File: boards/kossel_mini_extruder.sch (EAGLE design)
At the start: 31 parts

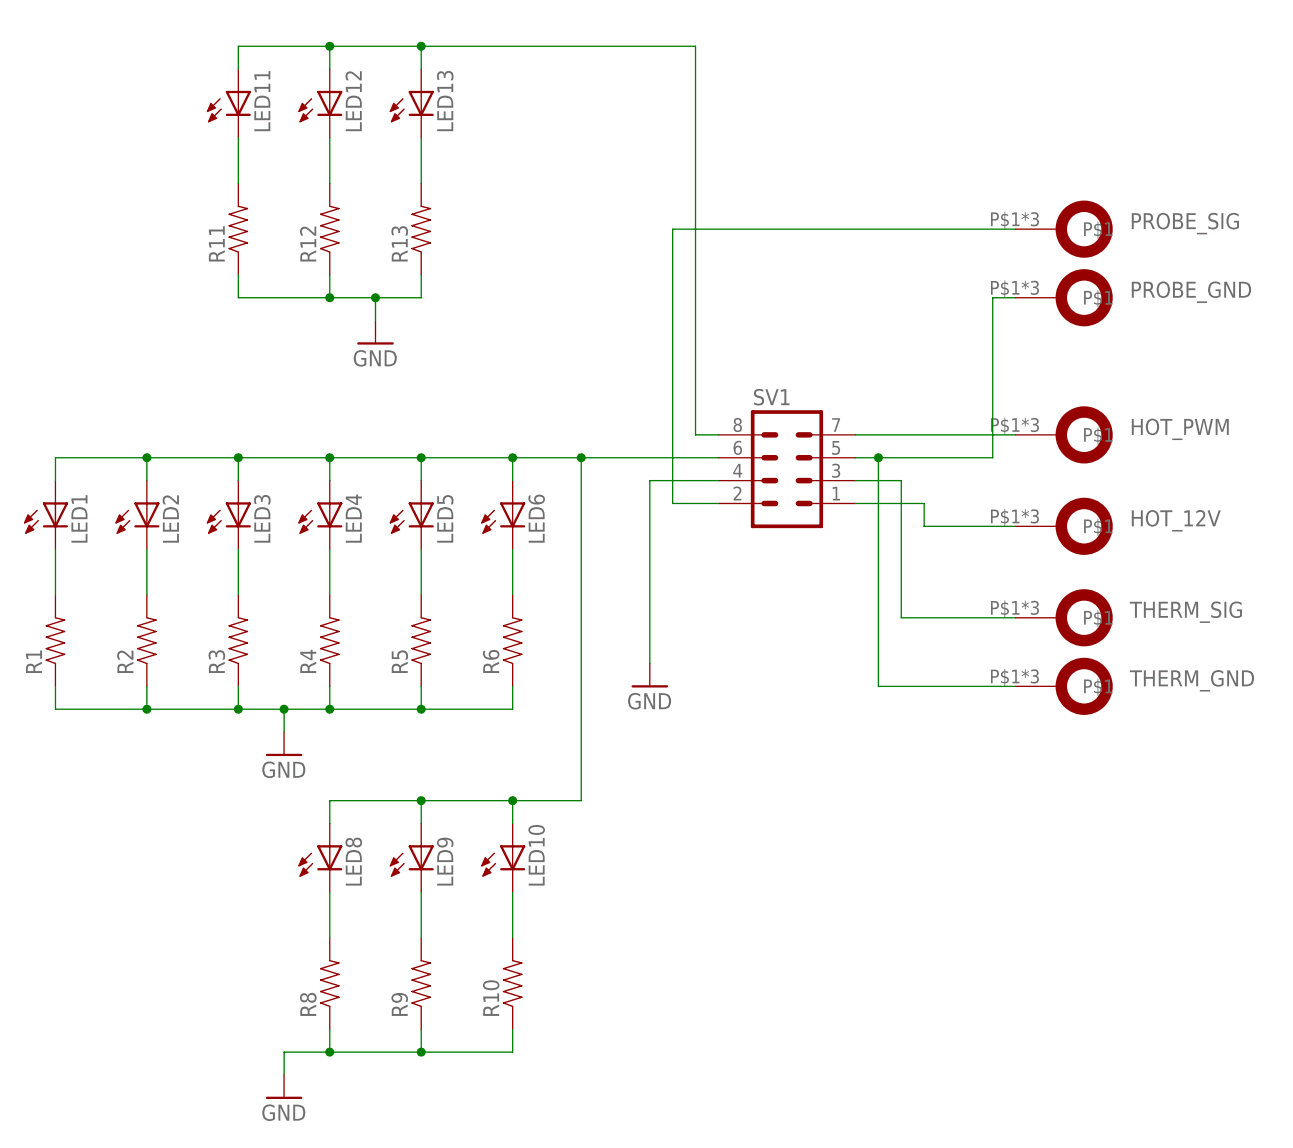
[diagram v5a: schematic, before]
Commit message: moved red leds onto hot end circuit
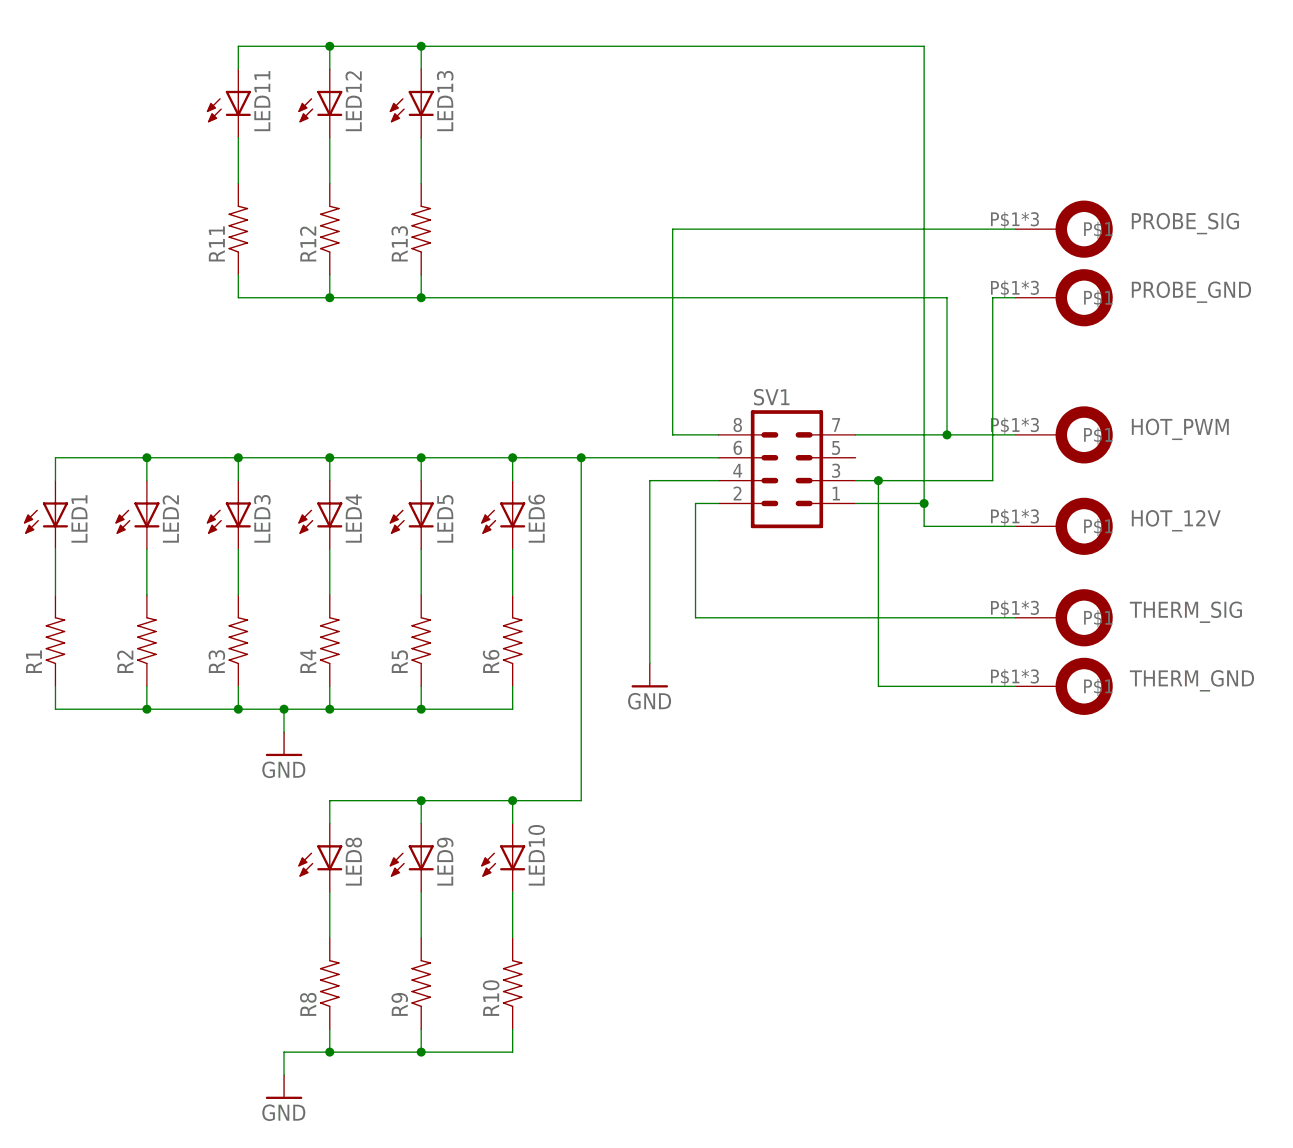
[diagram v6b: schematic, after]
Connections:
- removed net N$11: SV1.3, THERM_SIG.P$1
- removed net N$15: HOT_PWM.P$1, SV1.7
- new net N$7: HOT_PWM.P$1, R11.1, R12.1, R13.1, SV1.7
- net GND: no longer R11.1, R12.1, R13.1
- net N$10: now also SV1.2, THERM_SIG.P$1; no longer HOT_12V.P$1, SV1.1
- net N$20: now also SV1.8; no longer SV1.2
- net N$8: now also SV1.3; no longer SV1.5
- net VCC1: now also HOT_12V.P$1, SV1.1; no longer SV1.8
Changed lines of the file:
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@@
 <part name="R12" library="SparkFun-Passives" deviceset="RESISTOR" device="0805-RES"/>
 <part name="R13" library="SparkFun-Passives" deviceset="RESISTOR" device="0805-RES"/>
-<part name="GND2" library="SparkFun-Aesthetics" deviceset="GND" device=""/>
 </parts>
 <sheets>
@@
 <instance part="R12" gate="G$1" x="-12.7" y="101.6" rot="R90"/>
 <instance part="R13" gate="G$1" x="-2.54" y="101.6" rot="R90"/>
-<instance part="GND2" gate="1" x="-7.62" y="88.9"/>
 </instances>
 <busses>
@@
 <pinref part="GND1" gate="1" pin="GND"/>
 <wire x1="22.86" y1="53.34" x2="22.86" y2="73.66" width="0.1524" layer="91"/>
-</segment>
-<segment>
-<pinref part="R11" gate="G$1" pin="1"/>
-<wire x1="-22.86" y1="96.52" x2="-22.86" y2="93.98" width="0.1524" layer="91"/>
-<wire x1="-22.86" y1="93.98" x2="-12.7" y2="93.98" width="0.1524" layer="91"/>
-<wire x1="-12.7" y1="93.98" x2="-7.62" y2="93.98" width="0.1524" layer="91"/>
-<pinref part="R13" gate="G$1" pin="1"/>
-<wire x1="-7.62" y1="93.98" x2="-2.54" y2="93.98" width="0.1524" layer="91"/>
-<wire x1="-2.54" y1="96.52" x2="-2.54" y2="93.98" width="0.1524" layer="91"/>
-<pinref part="R12" gate="G$1" pin="1"/>
-<wire x1="-12.7" y1="96.52" x2="-12.7" y2="93.98" width="0.1524" layer="91"/>
-<junction x="-12.7" y="93.98"/>
-<pinref part="GND2" gate="1" pin="GND"/>
-<wire x1="-7.62" y1="91.44" x2="-7.62" y2="93.98" width="0.1524" layer="91"/>
-<junction x="-7.62" y="93.98"/>
 </segment>
 </net>
@@
 </segment>
 </net>
-<net name="N$11" class="0">
-<segment>
-<pinref part="THERM_SIG" gate="G$1" pin="P$1"/>
-<wire x1="63.5" y1="58.42" x2="50.8" y2="58.42" width="0.1524" layer="91"/>
-<pinref part="SV1" gate="G$1" pin="3"/>
-<wire x1="45.72" y1="73.66" x2="50.8" y2="73.66" width="0.1524" layer="91"/>
-<wire x1="50.8" y1="73.66" x2="50.8" y2="58.42" width="0.1524" layer="91"/>
-</segment>
-</net>
-<net name="N$15" class="0">
-<segment>
-<pinref part="HOT_PWM" gate="G$1" pin="P$1"/>
-<wire x1="45.72" y1="78.74" x2="63.5" y2="78.74" width="0.1524" layer="91"/>
-<pinref part="SV1" gate="G$1" pin="7"/>
-</segment>
-</net>
 <net name="N$8" class="0">
 <segment>
 <pinref part="THERM_GND" gate="G$1" pin="P$1"/>
 <wire x1="63.5" y1="50.8" x2="48.26" y2="50.8" width="0.1524" layer="91"/>
-<wire x1="48.26" y1="50.8" x2="48.26" y2="76.2" width="0.1524" layer="91"/>
-<pinref part="SV1" gate="G$1" pin="5"/>
-<wire x1="48.26" y1="76.2" x2="45.72" y2="76.2" width="0.1524" layer="91"/>
-<wire x1="48.26" y1="76.2" x2="60.96" y2="76.2" width="0.1524" layer="91"/>
+<wire x1="48.26" y1="50.8" x2="48.26" y2="73.66" width="0.1524" layer="91"/>
+<wire x1="48.26" y1="73.66" x2="60.96" y2="73.66" width="0.1524" layer="91"/>
 <pinref part="PROBE_GND" gate="G$1" pin="P$1"/>
 <wire x1="63.5" y1="93.98" x2="60.96" y2="93.98" width="0.1524" layer="91"/>
-<wire x1="60.96" y1="76.2" x2="60.96" y2="93.98" width="0.1524" layer="91"/>
-<junction x="48.26" y="76.2"/>
-</segment>
-</net>
-<net name="N$10" class="0">
-<segment>
-<pinref part="HOT_12V" gate="G$1" pin="P$1"/>
-<wire x1="53.34" y1="68.58" x2="63.5" y2="68.58" width="0.1524" layer="91"/>
-<wire x1="53.34" y1="68.58" x2="53.34" y2="71.12" width="0.1524" layer="91"/>
-<pinref part="SV1" gate="G$1" pin="1"/>
-<wire x1="45.72" y1="71.12" x2="53.34" y2="71.12" width="0.1524" layer="91"/>
+<wire x1="60.96" y1="73.66" x2="60.96" y2="93.98" width="0.1524" layer="91"/>
+<pinref part="SV1" gate="G$1" pin="3"/>
+<wire x1="45.72" y1="73.66" x2="48.26" y2="73.66" width="0.1524" layer="91"/>
+<junction x="48.26" y="73.66"/>
 </segment>
 </net>
@@
 <wire x1="-12.7" y1="119.38" x2="-12.7" y2="121.92" width="0.1524" layer="91"/>
 <junction x="-12.7" y="121.92"/>
-<pinref part="SV1" gate="G$1" pin="8"/>
-<wire x1="30.48" y1="78.74" x2="27.94" y2="78.74" width="0.1524" layer="91"/>
-<wire x1="27.94" y1="78.74" x2="27.94" y2="121.92" width="0.1524" layer="91"/>
-<wire x1="-2.54" y1="121.92" x2="27.94" y2="121.92" width="0.1524" layer="91"/>
+<wire x1="53.34" y1="121.92" x2="-2.54" y2="121.92" width="0.1524" layer="91"/>
 <junction x="-2.54" y="121.92"/>
+<pinref part="HOT_12V" gate="G$1" pin="P$1"/>
+<wire x1="53.34" y1="68.58" x2="63.5" y2="68.58" width="0.1524" layer="91"/>
+<wire x1="53.34" y1="68.58" x2="53.34" y2="71.12" width="0.1524" layer="91"/>
+<pinref part="SV1" gate="G$1" pin="1"/>
+<wire x1="45.72" y1="71.12" x2="53.34" y2="71.12" width="0.1524" layer="91"/>
+<wire x1="53.34" y1="121.92" x2="53.34" y2="71.12" width="0.1524" layer="91"/>
+<junction x="53.34" y="71.12"/>
 </segment>
 </net>
 <net name="N$20" class="0">
 <segment>
-<pinref part="SV1" gate="G$1" pin="2"/>
-<wire x1="25.4" y1="101.6" x2="25.4" y2="71.12" width="0.1524" layer="91"/>
-<wire x1="25.4" y1="71.12" x2="30.48" y2="71.12" width="0.1524" layer="91"/>
 <pinref part="PROBE_SIG" gate="G$1" pin="P$1"/>
 <wire x1="25.4" y1="101.6" x2="63.5" y2="101.6" width="0.1524" layer="91"/>
-</segment>
-</net>
+<wire x1="25.4" y1="101.6" x2="25.4" y2="78.74" width="0.1524" layer="91"/>
+<pinref part="SV1" gate="G$1" pin="8"/>
+<wire x1="25.4" y1="78.74" x2="30.48" y2="78.74" width="0.1524" layer="91"/>
+</segment>
+</net>
+<net name="N$7" class="0">
+<segment>
+<pinref part="R11" gate="G$1" pin="1"/>
+<wire x1="-22.86" y1="96.52" x2="-22.86" y2="93.98" width="0.1524" layer="91"/>
+<wire x1="-22.86" y1="93.98" x2="-12.7" y2="93.98" width="0.1524" layer="91"/>
+<pinref part="R13" gate="G$1" pin="1"/>
+<wire x1="-12.7" y1="93.98" x2="-2.54" y2="93.98" width="0.1524" layer="91"/>
+<wire x1="-2.54" y1="96.52" x2="-2.54" y2="93.98" width="0.1524" layer="91"/>
+<pinref part="R12" gate="G$1" pin="1"/>
+<wire x1="-12.7" y1="96.52" x2="-12.7" y2="93.98" width="0.1524" layer="91"/>
+<junction x="-12.7" y="93.98"/>
+<pinref part="HOT_PWM" gate="G$1" pin="P$1"/>
+<wire x1="45.72" y1="78.74" x2="55.88" y2="78.74" width="0.1524" layer="91"/>
+<pinref part="SV1" gate="G$1" pin="7"/>
+<wire x1="55.88" y1="78.74" x2="63.5" y2="78.74" width="0.1524" layer="91"/>
+<wire x1="-2.54" y1="93.98" x2="55.88" y2="93.98" width="0.1524" layer="91"/>
+<wire x1="55.88" y1="93.98" x2="55.88" y2="78.74" width="0.1524" layer="91"/>
+<junction x="55.88" y="78.74"/>
+<junction x="-2.54" y="93.98"/>
+</segment>
+</net>
+<net name="N$10" class="0">
+<segment>
+<pinref part="SV1" gate="G$1" pin="2"/>
+<wire x1="30.48" y1="71.12" x2="27.94" y2="71.12" width="0.1524" layer="91"/>
+<wire x1="27.94" y1="71.12" x2="27.94" y2="58.42" width="0.1524" layer="91"/>
+<pinref part="THERM_SIG" gate="G$1" pin="P$1"/>
+<wire x1="27.94" y1="58.42" x2="63.5" y2="58.42" width="0.1524" layer="91"/>
+</segment>
+</net>
